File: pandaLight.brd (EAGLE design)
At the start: 100 x 50 mm, 163 parts, among them J1 PJ-037A, U1 MIC23450AAAYML, U10 51, U11 TPD12S016PWR, U12 N25Q128AF8, U13 TPD12S016PWR, U14 AS4C128M16D3, U15 PMOD-2X6, U16 PMOD-2X6, U17 PLR135-T10, U18 PLT133-T10W, U19 PLR135-T10, U2 6SLX45CSG324, U20 TP10SQ, U21 TP10SQ, U22 PAN1322, U3 TPD4S014SON, U4 FT2232HL, U5 93LC46BT-I/OT, U6 51, U7 51, U8 TPD12S016PWR, U9 51, X1 USBUB-S, X2 HDMI_RECEPTICAL_A, X3 HDMI_RECEPTICAL_A, X4 HDMI_RECEPTICAL_A, Y1 403, Y2 20Mhz

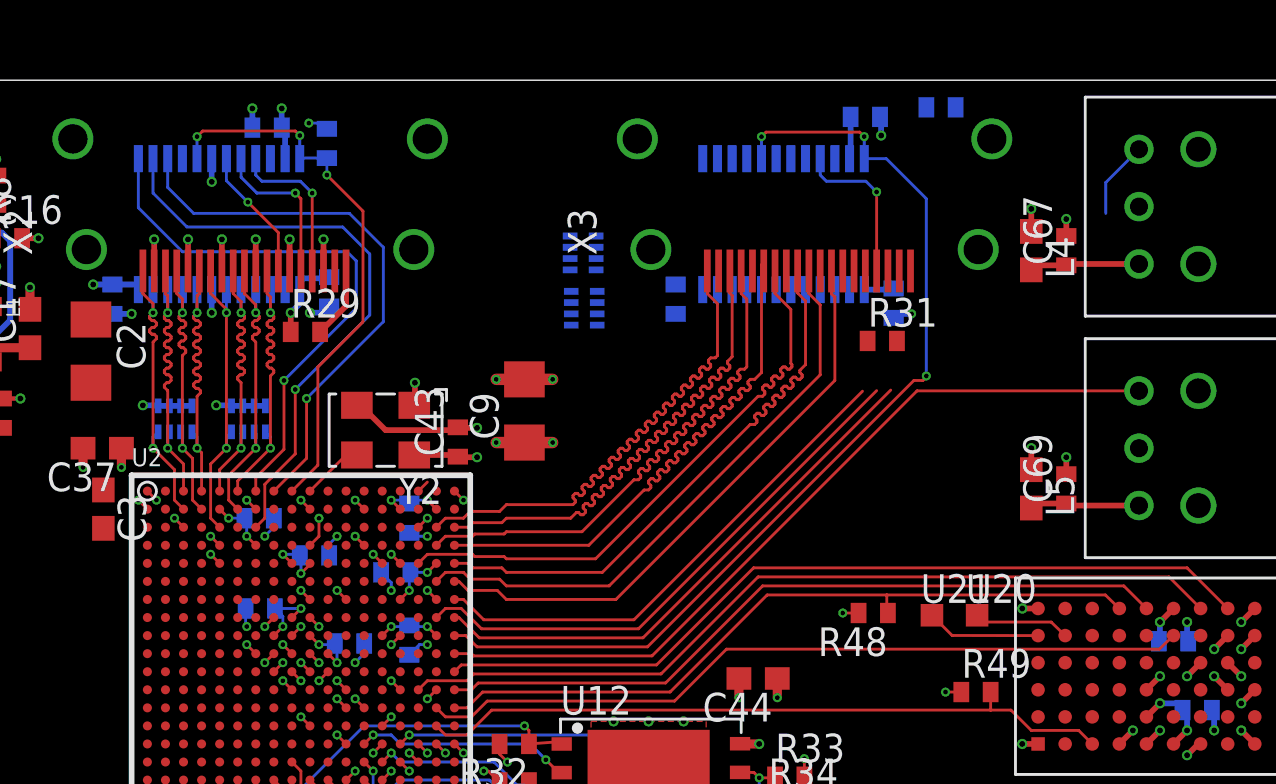
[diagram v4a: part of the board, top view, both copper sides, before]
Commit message: Finished putting the HDMI_RX1 traces on the top layer
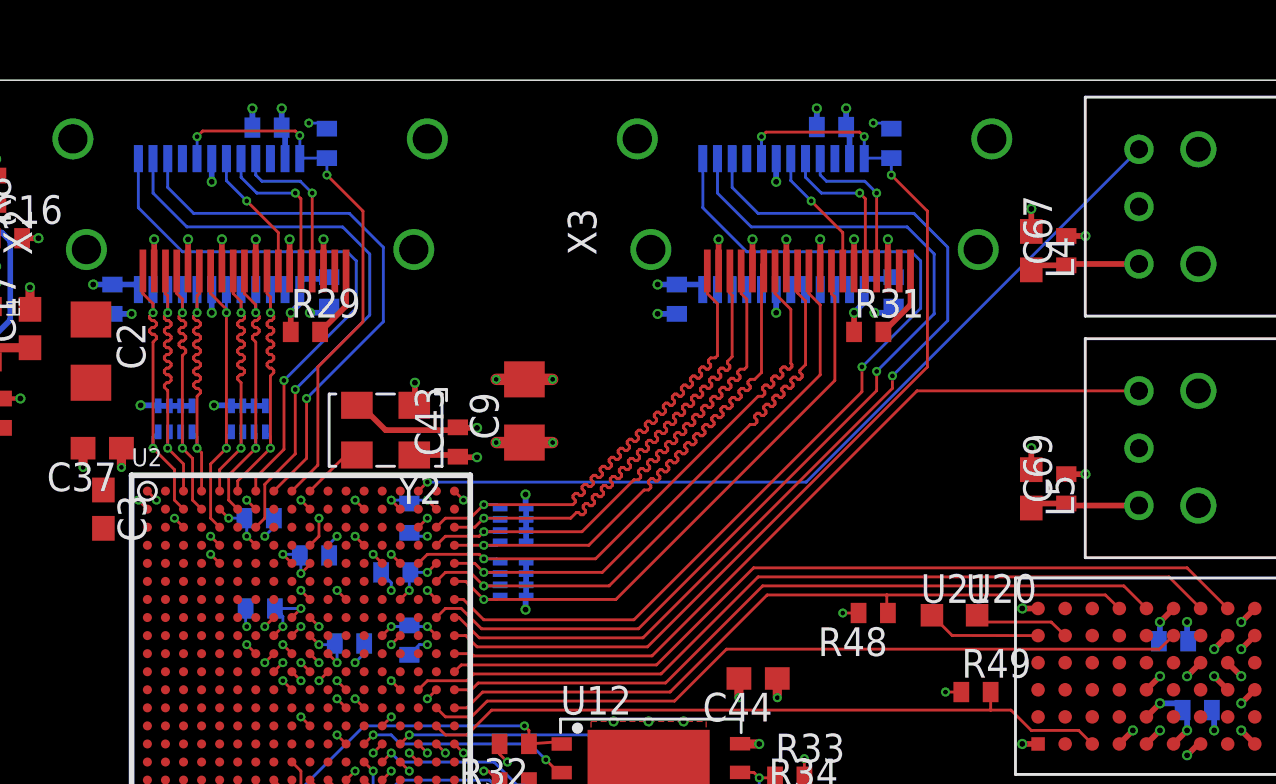
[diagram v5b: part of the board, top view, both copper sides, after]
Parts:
- moved U9 12.4 mm to (62.1, 30.3)
- moved U10 12.4 mm to (62.1, 27.9)
- moved R30 2.72 mm to (78.9, 47.2), turned to 270 degrees
- moved C48 1.57 mm to (76.2, 47.9), turned to 0 degrees
- moved R31 0.72 mm to (77.9, 38.9)
- moved C47 0.50 mm to (79.0, 40.6)
- moved C49 0.05 mm to (69.4, 40.3)
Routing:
- net TOS_IN0: track 4.01 -> 38.2 mm, vias 0 -> 1
- net HDMI_RX1_CEC_3V3: track 22.6 -> 42.3 mm, vias 0 -> 1
- net HDMI_RX1_SCL_3V3: track 24.4 -> 43.8 mm, vias 0 -> 1
- net HDMI_RX1_SDA_3V3: track 24.2 -> 43.5 mm, vias 0 -> 1
- net GND: track 144.4 -> 156.9 mm, vias 150 -> 160
- net HDMI_RX1_SCL_5V: track 0.00 -> 7.07 mm, vias 0 -> 1
- net +3V3: track 94.8 -> 101.4 mm, vias 69 -> 72
- net HDMI_RX1_CEC: track 0.00 -> 5.93 mm, vias 0 -> 1
- net N$37: track 0.00 -> 3.20 mm
- net HDMI_RX1_5V: track 1.32 -> 3.91 mm, vias 0 -> 1
- net HDMI_RX1_DATA1_N: track 26.8 -> 27.6 mm, vias 0 -> 1
- net HDMI_RX1_DATA0_P: track 26.1 -> 26.9 mm, vias 0 -> 1
- net HDMI_RX1_DATA2_P: track 25.9 -> 26.6 mm, vias 0 -> 1
- net HDMI_RX1_CLK_N: track 26.1 -> 26.9 mm, vias 0 -> 1
- net HDMI_RX1_DATA2_N: track 26.1 -> 26.8 mm, vias 0 -> 1
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
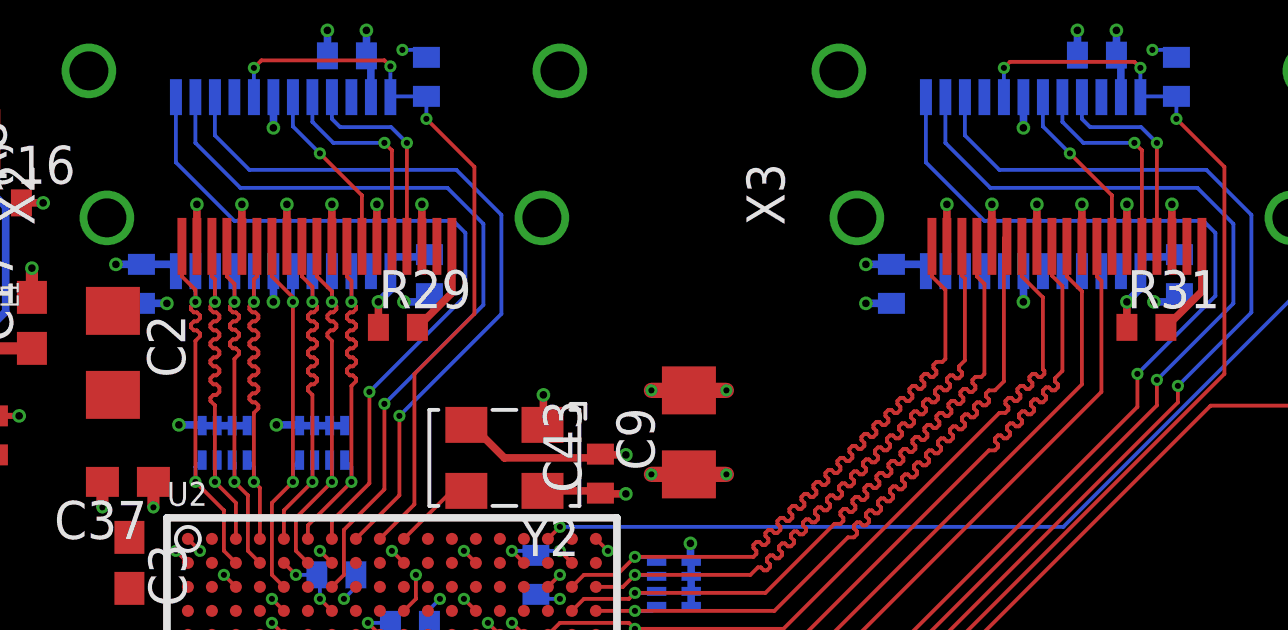
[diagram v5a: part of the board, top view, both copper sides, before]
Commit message: Forgot some vias at HDMI_RX1
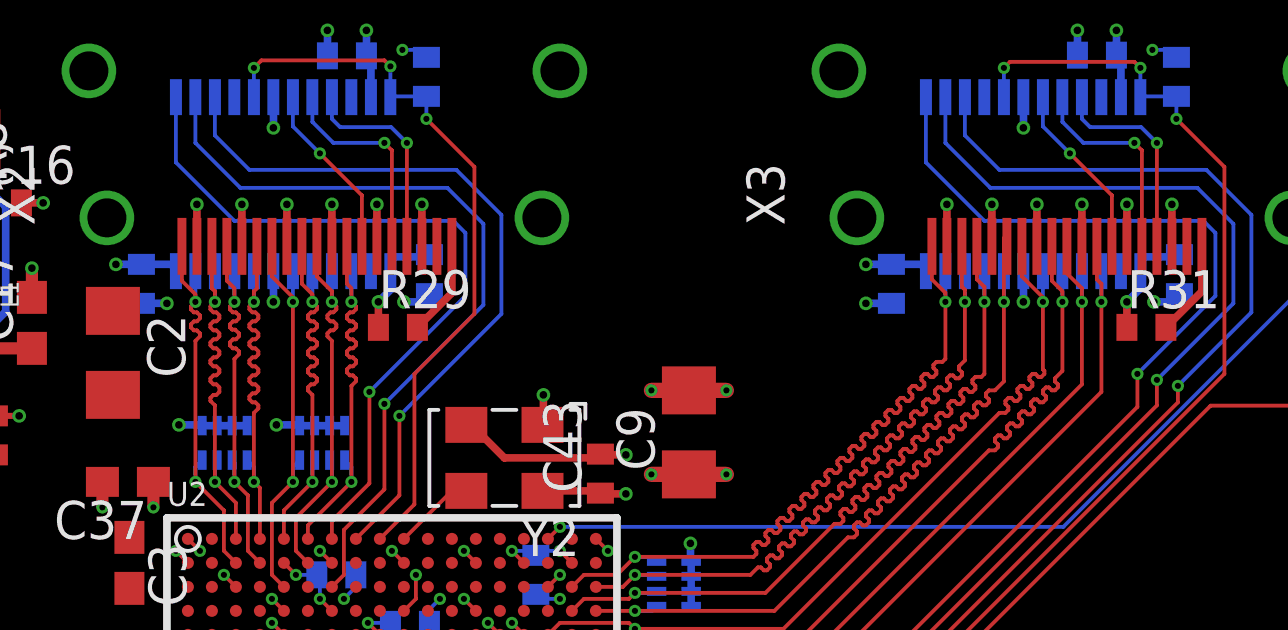
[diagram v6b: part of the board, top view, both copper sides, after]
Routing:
- net HDMI_RX1_DATA2_P: track 26.6 -> 27.7 mm, vias 1 -> 2
- net HDMI_RX1_DATA2_N: track 26.8 -> 27.8 mm, vias 1 -> 2
- net HDMI_RX1_DATA1_P: track 26.8 -> 27.9 mm, vias 1 -> 2
- net HDMI_RX1_DATA1_N: track 27.6 -> 28.6 mm, vias 1 -> 2
- net HDMI_RX1_DATA0_P: track 26.9 -> 27.9 mm, vias 1 -> 2
- net HDMI_RX1_DATA0_N: track 26.9 -> 27.9 mm, vias 1 -> 2
- net HDMI_RX1_CLK_P: track 26.8 -> 27.9 mm, vias 1 -> 2
- net HDMI_RX1_CLK_N: track 26.9 -> 27.9 mm, vias 1 -> 2

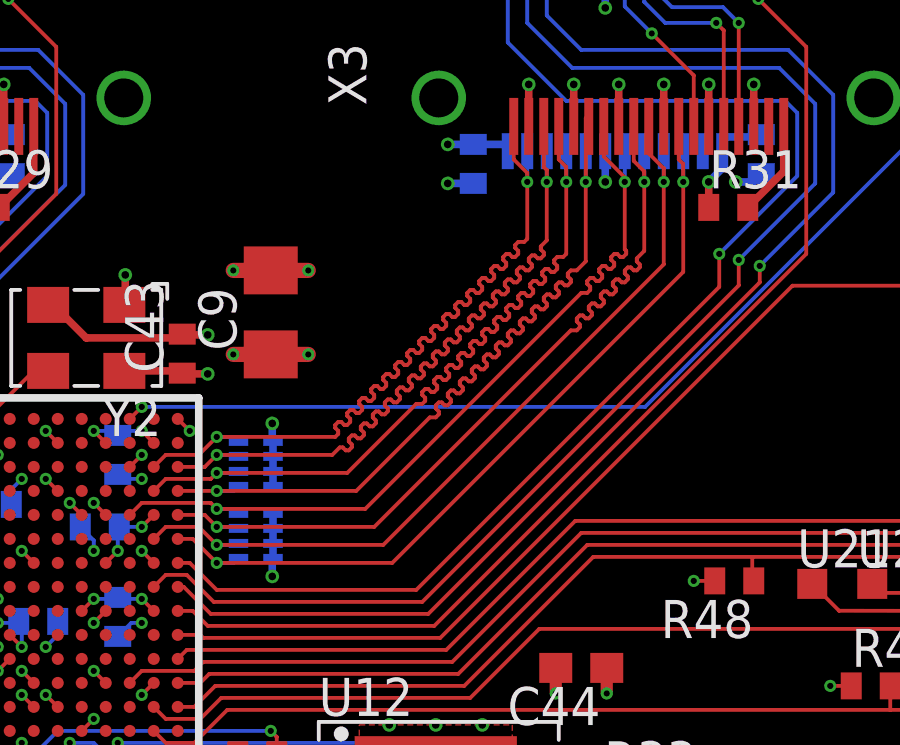
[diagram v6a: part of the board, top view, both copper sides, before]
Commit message: Tried the differential routing and the meander
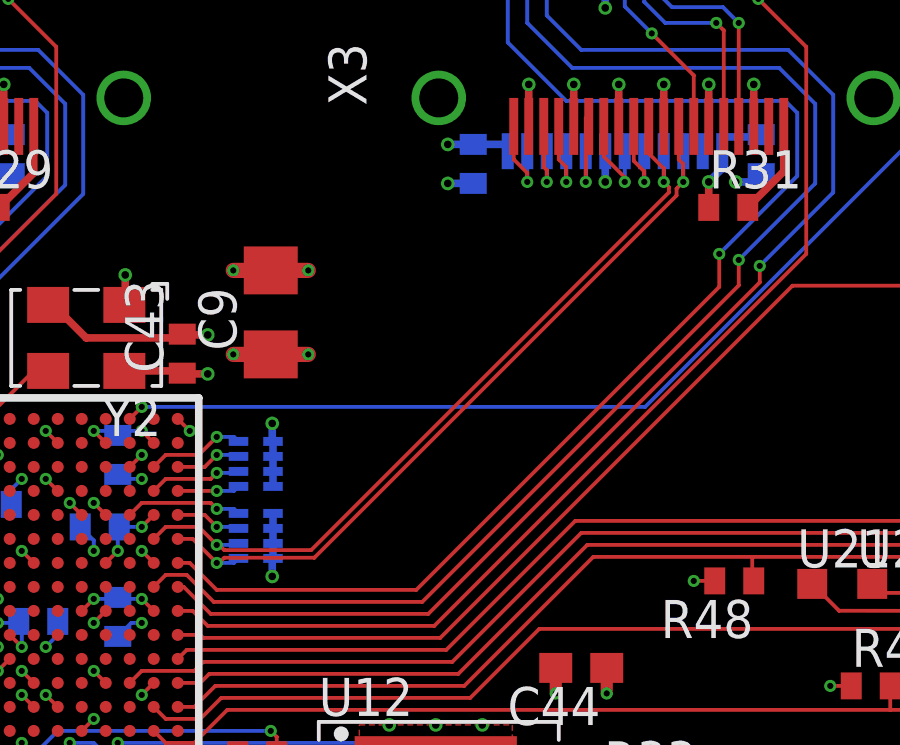
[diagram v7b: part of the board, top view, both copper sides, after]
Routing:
- net HDMI_RX1_DATA1_N: track 28.6 -> 5.75 mm
- net HDMI_RX1_DATA0_N: track 27.9 -> 5.23 mm
- net HDMI_RX1_DATA2_N: track 27.8 -> 5.23 mm
- net HDMI_RX1_DATA1_P: track 27.9 -> 6.07 mm
- net HDMI_RX1_DATA2_P: track 27.7 -> 6.36 mm
- net HDMI_RX1_DATA0_P: track 27.9 -> 7.10 mm
- net HDMI_RX1_CLK_N: track 27.9 -> 26.3 mm
- net HDMI_RX1_CLK_P: track 27.9 -> 26.8 mm

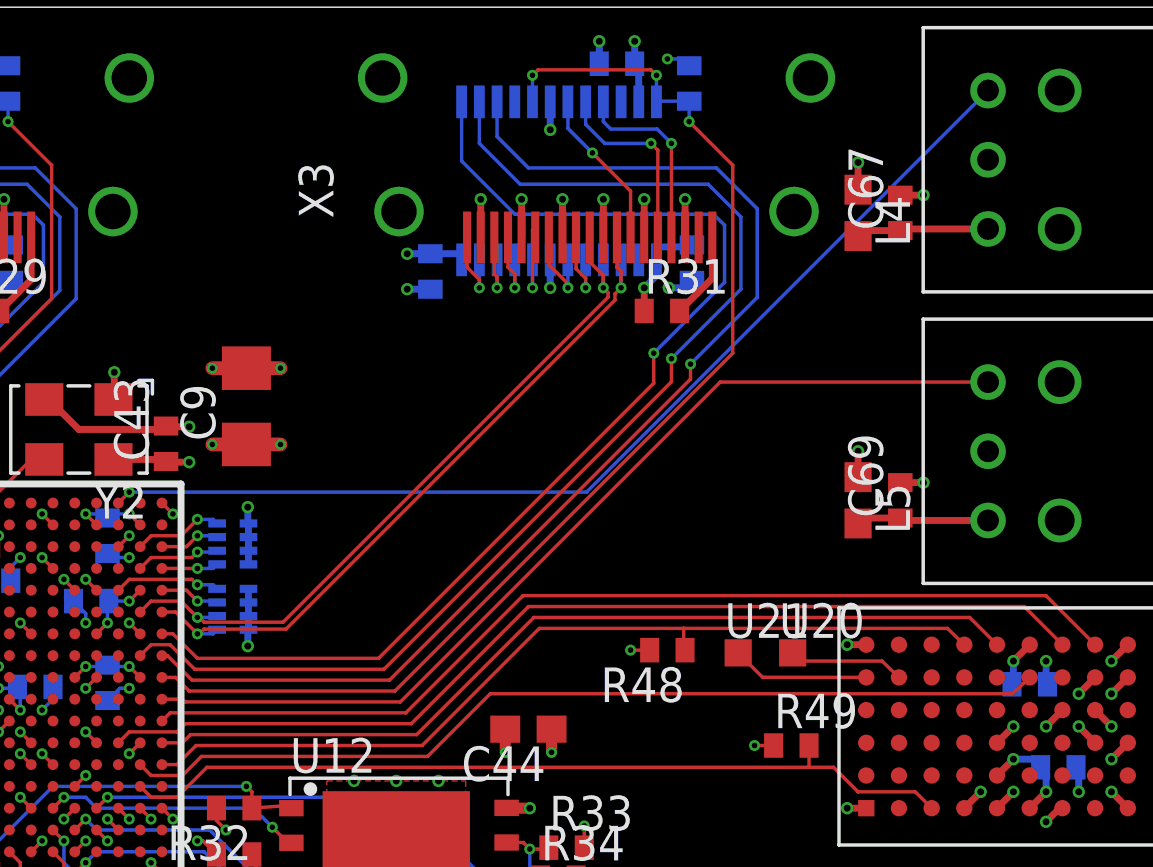
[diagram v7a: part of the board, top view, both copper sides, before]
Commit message: Used the meander on the HDMI_RX1 traces
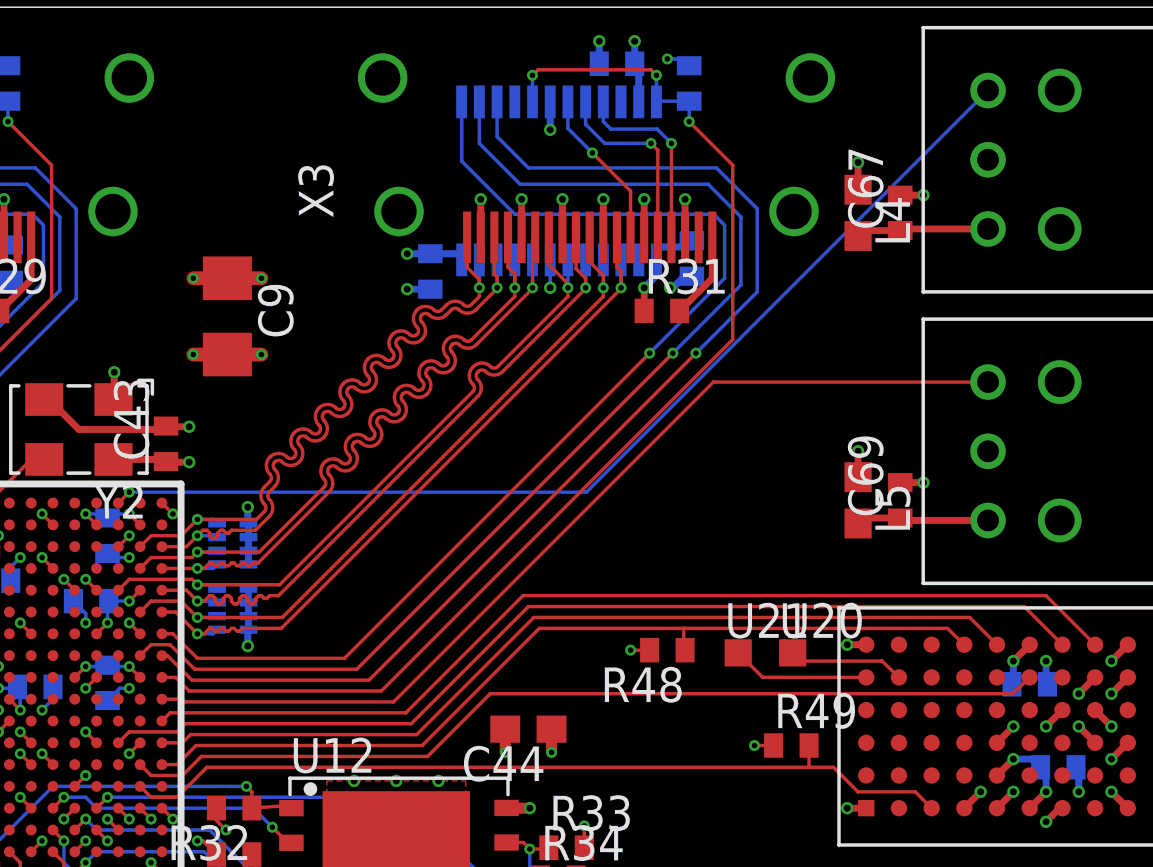
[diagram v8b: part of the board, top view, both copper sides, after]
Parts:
- moved C9 3.37 mm to (62.0, 38.6), turned to 270 degrees
- moved C47 0.15 mm to (79.0, 40.8)
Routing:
- net HDMI_RX1_DATA0_N: track 5.23 -> 26.0 mm
- net HDMI_RX1_DATA2_N: track 5.23 -> 24.6 mm
- net HDMI_RX1_DATA1_N: track 5.75 -> 25.1 mm
- net HDMI_RX1_DATA1_P: track 6.07 -> 25.1 mm
- net HDMI_RX1_DATA0_P: track 7.10 -> 25.9 mm
- net HDMI_RX1_DATA2_P: track 6.36 -> 24.6 mm
- net HDMI_RX1_CEC_3V3: track 42.3 -> 41.5 mm
- net HDMI_RX1_SCL_3V3: track 43.8 -> 43.2 mm
